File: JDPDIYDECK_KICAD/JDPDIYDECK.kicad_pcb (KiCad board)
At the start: 2 copper layers, 55.5 x 96.5 mm, 417 parts, among them J1 Conn_01x05, J2 Conn_01x05, J3 Conn_01x02, U1 NSL-32, U2 NSL-32, U3 TLV2372

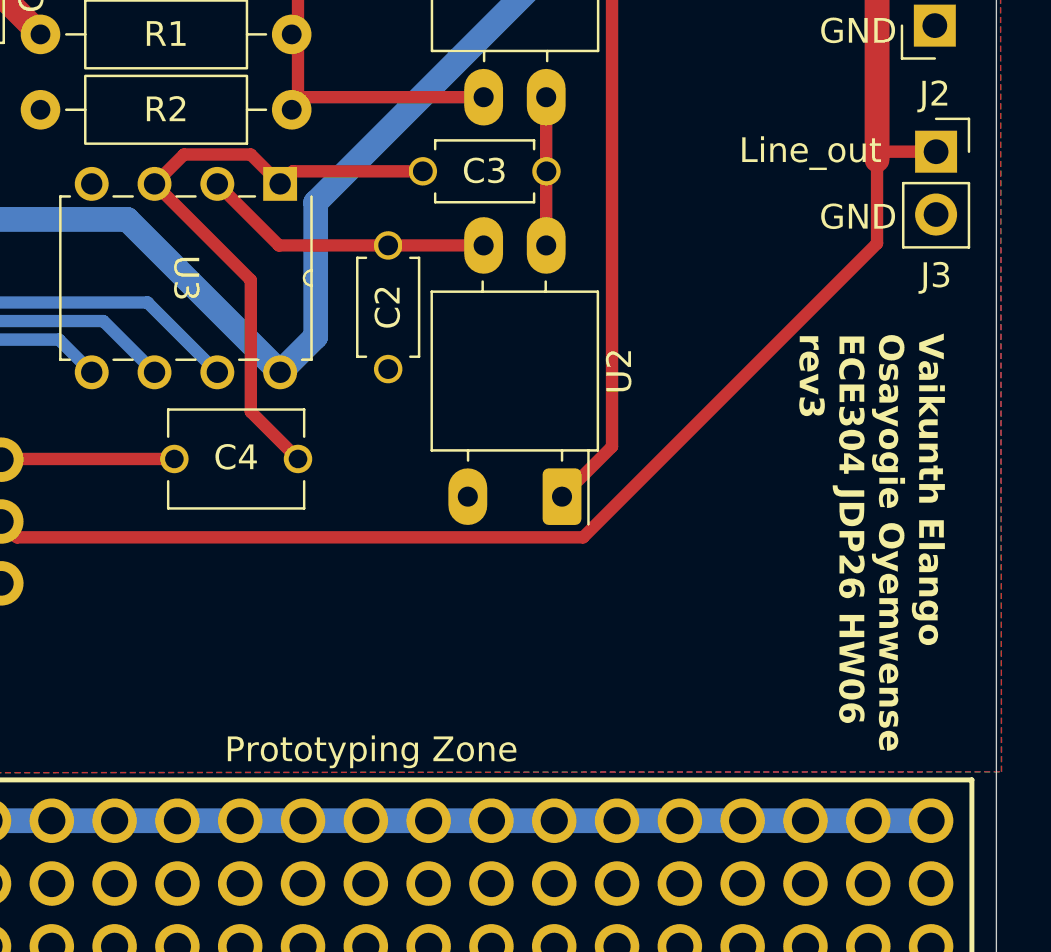
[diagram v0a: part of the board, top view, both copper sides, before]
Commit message: amendments to op amp routing
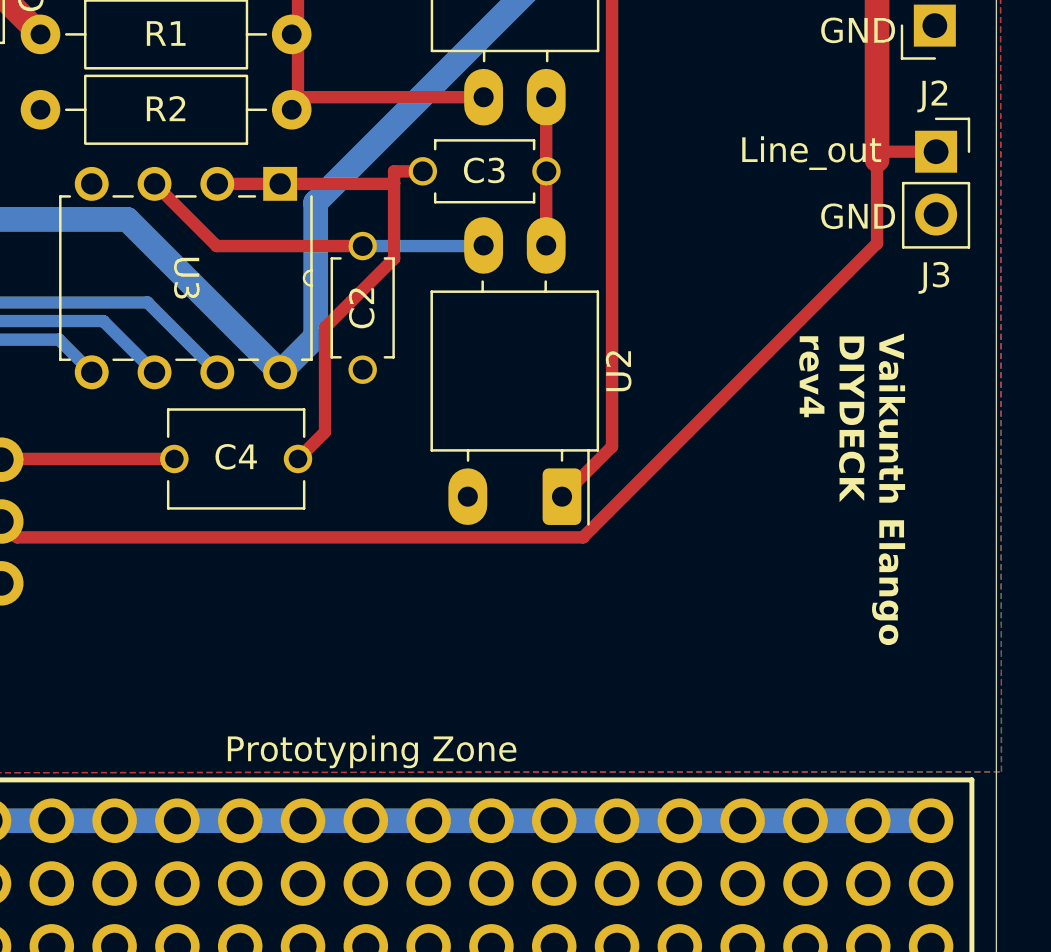
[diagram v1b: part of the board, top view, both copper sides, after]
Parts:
- moved C2 1.03 mm to (148.5, 75.8)
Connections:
- C2 pad 1: Net-(U3A--) -> Net-(U3A-+)
- C3 pad 1: Net-(U3A-+) -> Net-(U3A--)
- C4 pad 1: Net-(U3A-+) -> Net-(U3A--)
- U2 pad 3: Net-(U3A--) -> Net-(U3A-+)
- U3 pad 1: Net-(U3A-+) -> Net-(U3A--)
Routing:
- net Net-(U3A-+): track 25.6 -> 14.4 mm
- net Net-(U3A--): track 11.8 -> 21.6 mm
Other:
- board text added: "Vaikunth Elango DIYDECK rev4"
- board text removed: "Vaikunth Elango Osayogie Oyemwense ECE304 JDP26 HW06 rev3"
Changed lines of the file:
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@@
 	(title_block
 		(title "ECE304_HW06")
-		(date "2026-04-01")
-		(rev "rev3")
-		(company "ECE 304 JDP26")
-		(comment 1 "Osayogie Oyemwense")
-		(comment 2 "Vaikunth Elango")
+		(date "2026-05-16")
+		(rev "rev4")
+		(company "Vaikunth Elango")
 	)
 	(layers
@@
 		(property ki_fp_filters "Luna*NSL?32*")
 		(sheetname "/")
-		(sheetfile "ECE304_HW05.kicad_sch")
+		(sheetfile "JDPDIYDECK.kicad_sch")
 		(attr through_hole)
 		(fp_line
@@
 			(layers "*.Cu" "*.Mask")
 			(remove_unused_layers no)
-			(net 3 "Net-(U3A--)")
+			(net 6 "Net-(U3A-+)")
 			(pinfunction "R")
 			(pintype "passive")
@@
 		(property ki_fp_filters "R_*")
 		(sheetname "/")
-		(sheetfile "ECE304_HW05.kicad_sch")
+		(sheetfile "JDPDIYDECK.kicad_sch")
 		(attr through_hole)
 		(fp_line
@@
 		(property ki_fp_filters "R_*")
 		(sheetname "/")
-		(sheetfile "ECE304_HW05.kicad_sch")
+		(sheetfile "JDPDIYDECK.kicad_sch")
 		(attr through_hole)
 		(fp_line
@@
 		(property ki_fp_filters "SOIC*3.9x4.9mm*P1.27mm* DIP*W7.62mm* TO*99* OnSemi*Micro8* TSSOP*3x3mm*P0.65mm* TSSOP*4.4x3mm*P0.65mm* MSOP*3x3mm*P0.65mm* SSOP*3.9x4.9mm*P0.635mm* LFCSP*2x2mm*P0.5mm* *SIP* SOIC*5.3x6.2mm*P1.27mm*")
 		(sheetname "/")
-		(sheetfile "ECE304_HW05.kicad_sch")
+		(sheetfile "JDPDIYDECK.kicad_sch")
 		(attr through_hole)
 		(fp_line
@@
 			(layers "*.Cu" "*.Mask")
 			(remove_unused_layers no)
-			(net 6 "Net-(U3A-+)")
+			(net 3 "Net-(U3A--)")
 			(pintype "output")
 		)
@@
 		(property ki_fp_filters "Potentiometer*")
 		(sheetname "/")
-		(sheetfile "ECE304_HW05.kicad_sch")
+		(sheetfile "JDPDIYDECK.kicad_sch")
 		(attr through_hole)
 		(fp_line
@@
 		(property ki_fp_filters "C_*")
 		(sheetname "/")
-		(sheetfile "ECE304_HW05.kicad_sch")
+		(sheetfile "JDPDIYDECK.kicad_sch")
 		(attr through_hole)
 		(fp_line
@@
 			(layers "*.Cu" "*.Mask")
 			(remove_unused_layers no)
-			(net 6 "Net-(U3A-+)")
+			(net 3 "Net-(U3A--)")
 			(pintype "passive")
 			(solder_mask_margin 0.102)
@@
 		(property ki_fp_filters "Luna*NSL?32*")
 		(sheetname "/")
-		(sheetfile "ECE304_HW05.kicad_sch")
+		(sheetfile "JDPDIYDECK.kicad_sch")
 		(attr through_hole)
 		(fp_line
@@
 		(property ki_fp_filters "CP_*")
 		(sheetname "/")
-		(sheetfile "ECE304_HW05.kicad_sch")
+		(sheetfile "JDPDIYDECK.kicad_sch")
 		(attr through_hole)
 		(fp_line
@@
 		(property ki_fp_filters "R_*")
 		(sheetname "/")
-		(sheetfile "ECE304_HW05.kicad_sch")
+		(sheetfile "JDPDIYDECK.kicad_sch")
 		(attr through_hole)
 		(fp_line
@@
 		(property ki_fp_filters "R_*")
 		(sheetname "/")
-		(sheetfile "ECE304_HW05.kicad_sch")
+		(sheetfile "JDPDIYDECK.kicad_sch")
 		(attr through_hole)
 		(fp_line
@@
 	(footprint "FA28X7R1H472KNU00:CAPRB500W50L400T250H550"
 		(layer "F.Cu")
-		(at 149.4936 75.7536 -90)
+		(at 148.463 75.779 -90)
 		(property "Reference" "C2"
 			(at -0.0108 0 90)
@@
 		(property ki_fp_filters "C_*")
 		(sheetname "/")
-		(sheetfile "ECE304_HW05.kicad_sch")
+		(sheetfile "JDPDIYDECK.kicad_sch")
 		(attr through_hole)
 		(fp_line
@@
 			(layers "*.Cu" "*.Mask")
 			(remove_unused_layers no)
-			(net 3 "Net-(U3A--)")
+			(net 6 "Net-(U3A-+)")
 			(pintype "passive")
 			(solder_mask_margin 0.102)
@@
 		(property ki_fp_filters "Connector*:*_1x??_*")
 		(sheetname "/")
-		(sheetfile "ECE304_HW05.kicad_sch")
+		(sheetfile "JDPDIYDECK.kicad_sch")
 		(attr through_hole)
 		(fp_line
@@
 		(property ki_fp_filters "C_*")
 		(sheetname "/")
-		(sheetfile "ECE304_HW05.kicad_sch")
+		(sheetfile "JDPDIYDECK.kicad_sch")
 		(attr through_hole)
 		(fp_line
@@
 		(property ki_fp_filters "C_*")
 		(sheetname "/")
-		(sheetfile "ECE304_HW05.kicad_sch")
+		(sheetfile "JDPDIYDECK.kicad_sch")
 		(attr through_hole)
 		(fp_line
@@
 		(property ki_fp_filters "Connector*:*_1x??_*")
 		(sheetname "/")
-		(sheetfile "ECE304_HW05.kicad_sch")
+		(sheetfile "JDPDIYDECK.kicad_sch")
 		(attr through_hole)
 		(fp_line
@@
 		(property ki_fp_filters "Connector*:*_1x??_*")
 		(sheetname "/")
-		(sheetfile "ECE304_HW05.kicad_sch")
+		(sheetfile "JDPDIYDECK.kicad_sch")
 		(attr through_hole)
 		(fp_line
@@
 		(property ki_fp_filters "C_*")
 		(sheetname "/")
-		(sheetfile "ECE304_HW05.kicad_sch")
+		(sheetfile "JDPDIYDECK.kicad_sch")
 		(attr through_hole)
 		(fp_line
@@
 			(layers "*.Cu" "*.Mask")
 			(remove_unused_layers no)
-			(net 6 "Net-(U3A-+)")
+			(net 3 "Net-(U3A--)")
 			(pintype "passive")
 			(solder_mask_margin 0.102)
@@
 		)
 	)
-	(gr_text "Vaikunth Elango\nOsayogie Oyemwense\nECE304 JDP26 HW06\nrev3\n"
+	(gr_text "Vaikunth Elango\nDIYDECK\nrev4\n"
 		(at 166.0144 76.8096 270)
 		(layer "F.SilkS")
@@
 	)
 	(segment
-		(start 149.4936 73.2536)
-		(end 145.074 73.2536)
+		(start 142.5848 70.7644)
+		(end 145.1248 70.7644)
 		(width 0.5)
 		(layer "F.Cu")
@@
 	)
 	(segment
-		(start 149.4936 73.2536)
-		(end 153.3544 73.2536)
+		(start 146.939 80.7974)
+		(end 146.939 76.581)
+		(width 0.5)
+		(layer "F.Cu")
+		(net 3)
+	)
+	(segment
+		(start 150.8952 70.2564)
+		(end 149.733 70.2564)
+		(width 0.5)
+		(layer "F.Cu")
+		(net 3)
+	)
+	(segment
+		(start 145.8468 81.8896)
+		(end 146.939 80.7974)
+		(width 0.5)
+		(layer "F.Cu")
+		(net 3)
+	)
+	(segment
+		(start 149.733 73.787)
+		(end 149.733 70.739)
 		(width 0.5)
 		(layer "F.Cu")
@@
 	)
 	(segment
-		(start 145.074 73.2536)
-		(end 142.5848 70.7644)
+		(start 149.733 70.739)
+		(end 149.733 70.2564)
+		(width 0.5)
+		(layer "F.Cu")
+		(net 3)
+	)
+	(segment
+		(start 149.7076 70.7644)
+		(end 149.733 70.739)
+		(width 0.5)
+		(layer "F.Cu")
+		(net 3)
+	)
+	(segment
+		(start 146.939 76.581)
+		(end 149.733 73.787)
+		(width 0.5)
+		(layer "F.Cu")
+		(net 3)
+	)
+	(segment
+		(start 145.1248 70.7644)
+		(end 149.7076 70.7644)
 		(width 0.5)
 		(layer "F.Cu")
@@
 	)
 	(segment
-		(start 145.8468 81.8896)
-		(end 143.938 79.9808)
+		(start 148.463 73.279)
+		(end 142.5594 73.279)
 		(width 0.5)
 		(layer "F.Cu")
@@
 	)
 	(segment
-		(start 143.938 69.5776)
-		(end 145.1248 70.7644)
-		(width 0.5)
-		(layer "F.Cu")
-		(net 6)
-	)
-	(segment
-		(start 141.2316 69.5776)
-		(end 143.938 69.5776)
-		(width 0.5)
-		(layer "F.Cu")
-		(net 6)
-	)
-	(segment
-		(start 140.0448 70.7644)
-		(end 141.2316 69.5776)
-		(width 0.5)
-		(layer "F.Cu")
-		(net 6)
-	)
-	(segment
-		(start 143.938 79.9808)
-		(end 143.938 74.6576)
-		(width 0.5)
-		(layer "F.Cu")
-		(net 6)
-	)
-	(segment
-		(start 145.6328 70.2564)
-		(end 145.1248 70.7644)
+		(start 142.5594 73.279)
+		(end 140.0448 70.7644)
 		(width 0.5)
 		(layer "F.Cu")
@@
 	)
 	(segment
-		(start 143.938 74.6576)
-		(end 140.0448 70.7644)
+		(start 148.463 73.279)
+		(end 153.329 73.279)
 		(width 0.5)
-		(layer "F.Cu")
+		(layer "B.Cu")
 		(net 6)
 	)
 	(segment
-		(start 150.8952 70.2564)
-		(end 145.6328 70.2564)
+		(start 153.329 73.279)
+		(end 153.3544 73.2536)
 		(width 0.5)
-		(layer "F.Cu")
+		(layer "B.Cu")
 		(net 6)
 	)
